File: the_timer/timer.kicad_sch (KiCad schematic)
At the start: 23 parts, among them J1 AVR-ISP-6, J2 Conn_01x04_Socket, J3 Conn_01x02_Socket, Q1 2N7002, Q2 2N7002, Q3 2N7002, U1 ATtiny48-A, U2 TPS61033, U3 MC3416, U4 W25Q128JVS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

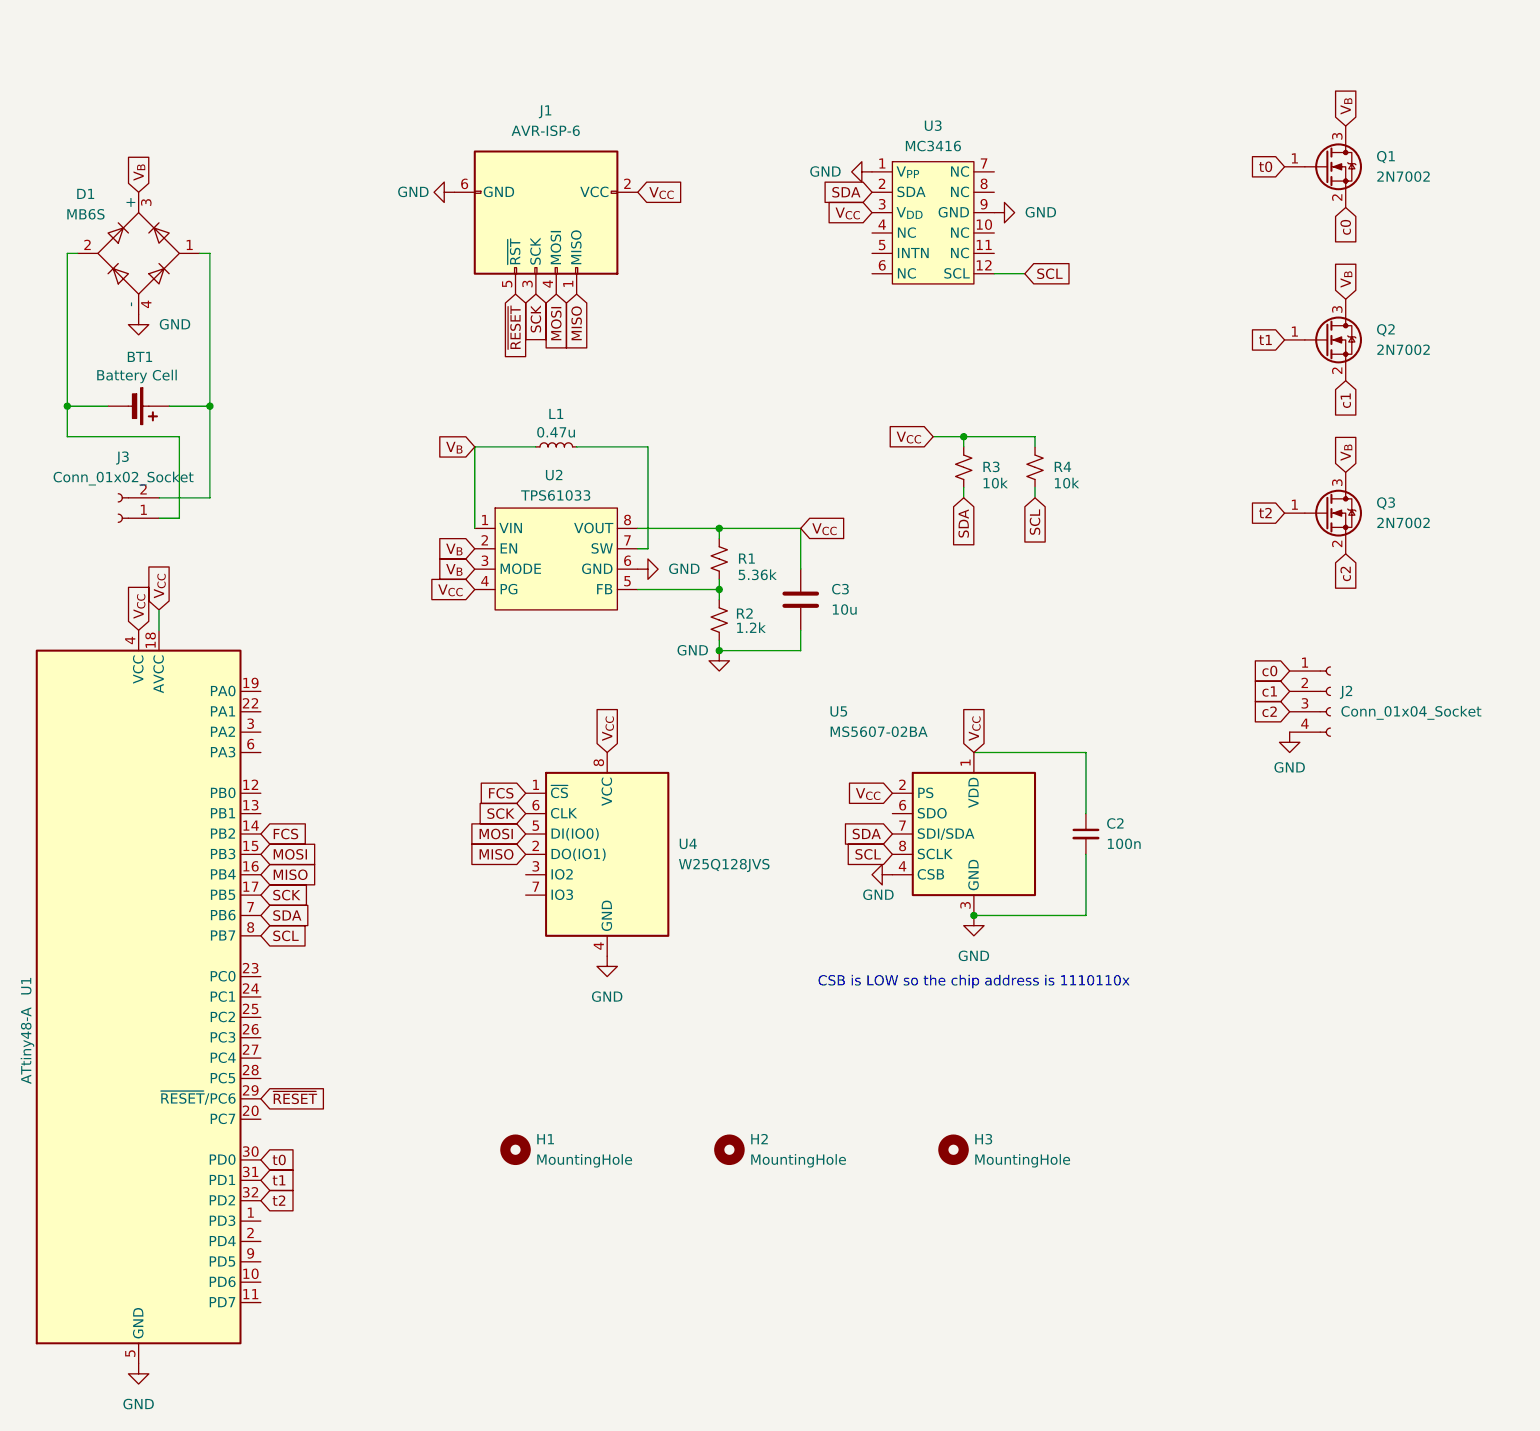
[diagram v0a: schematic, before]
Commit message: Replaced Timer mosfets
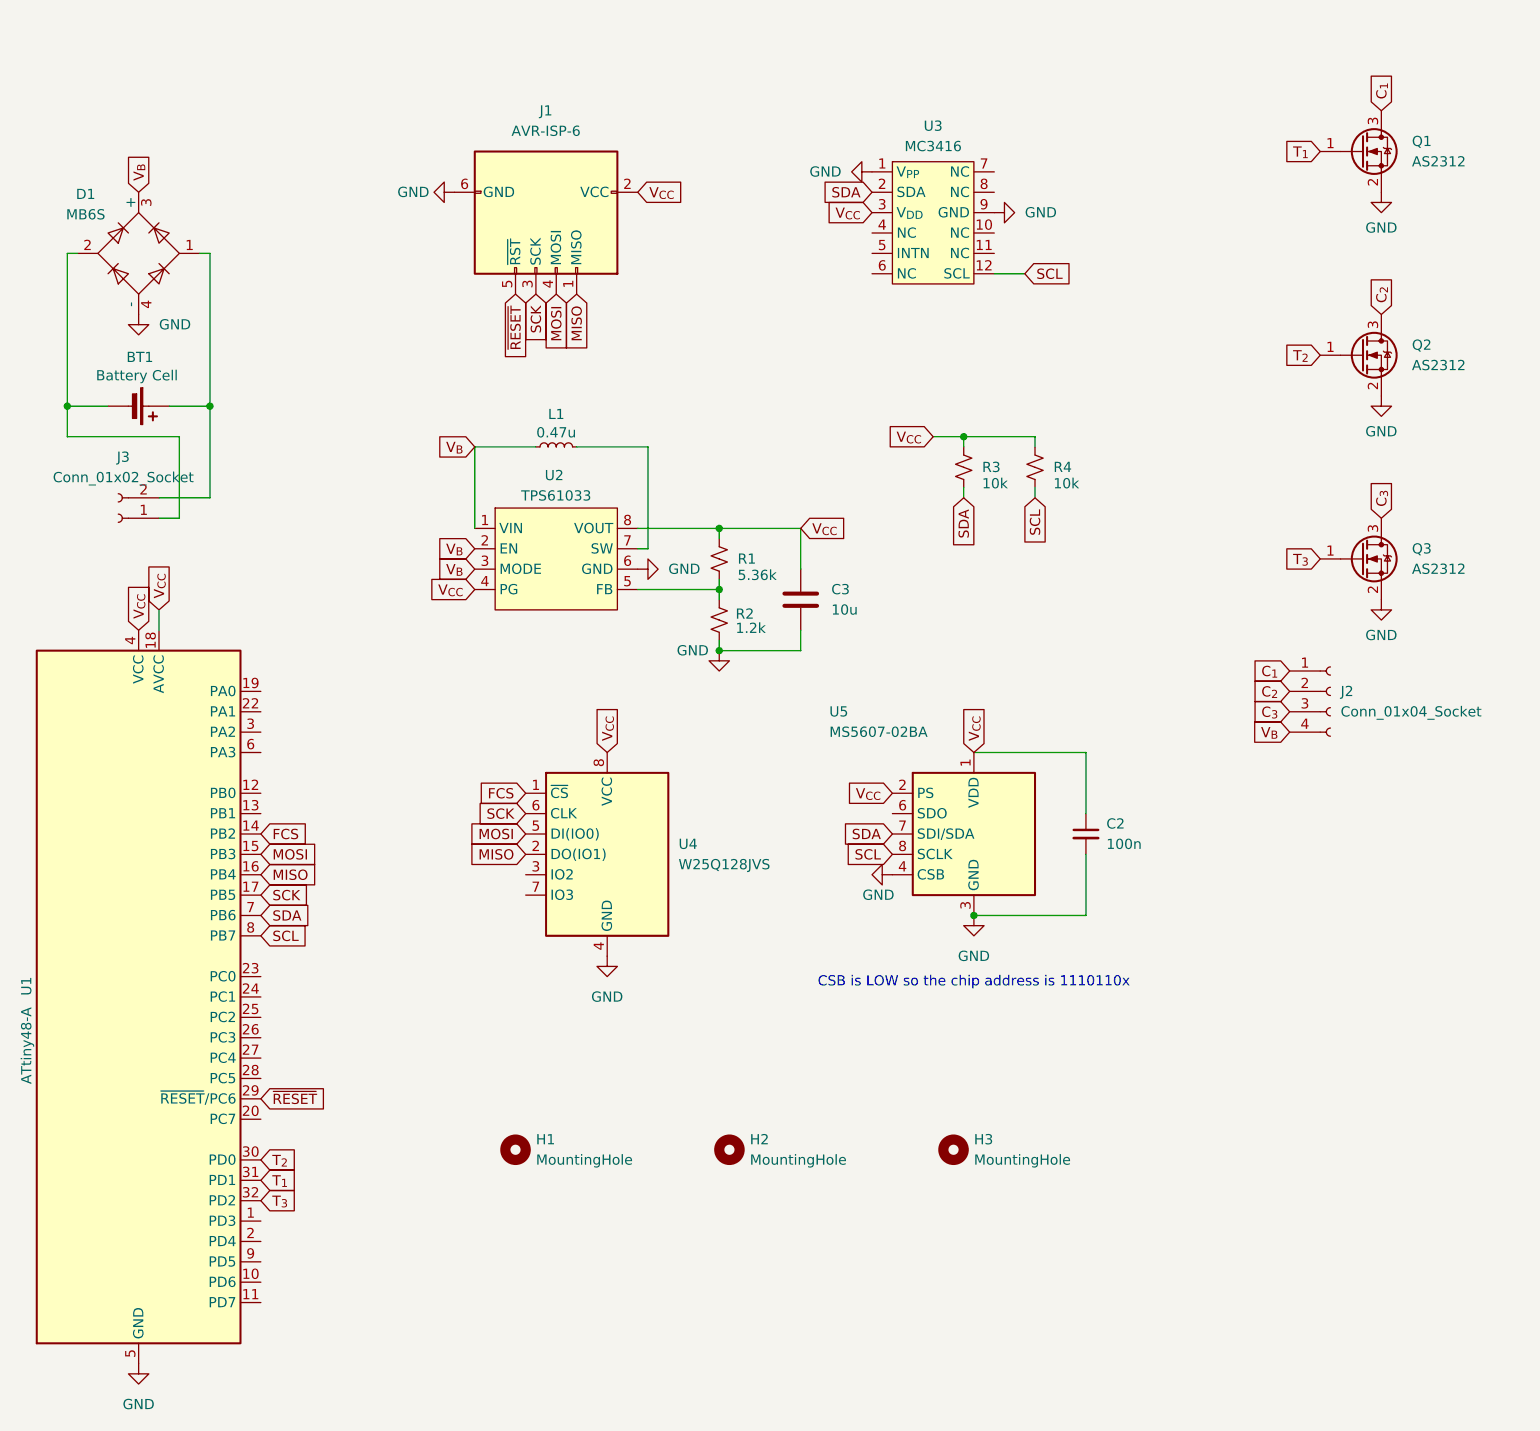
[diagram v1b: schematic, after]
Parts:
- Q1, Q2, Q3: value 2N7002 -> AS2312; DKPN 2N7002NCT-ND -> 4530-AS2312CT-ND
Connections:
- net GND: now also Q1.2 (S), Q2.2 (S), Q3.2 (S); no longer J2.4 (Pin_4)
- net V_{B}: now also J2.4 (Pin_4); no longer Q1.3 (D), Q2.3 (D), Q3.3 (D)
- net c0 renamed C_{1}
- net C_{1}: now also Q1.3 (D); no longer Q1.2 (S)
- net c1 renamed C_{2}
- net C_{2}: now also Q2.3 (D); no longer Q2.2 (S)
- net c2 renamed C_{3}
- net C_{3}: now also Q3.3 (D); no longer Q3.2 (S)
- net t0 renamed T_{1}
- net T_{1}: now also U1.31 (PD1); no longer U1.30 (PD0)
- net t1 renamed T_{2}
- net T_{2}: now also U1.30 (PD0); no longer U1.31 (PD1)
- net t2 renamed T_{3}
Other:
- moved on the sheet: Q1

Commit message: Generated Screamer and Timer BOMs
Both Screamer and Timer have been bumped to V0.1.
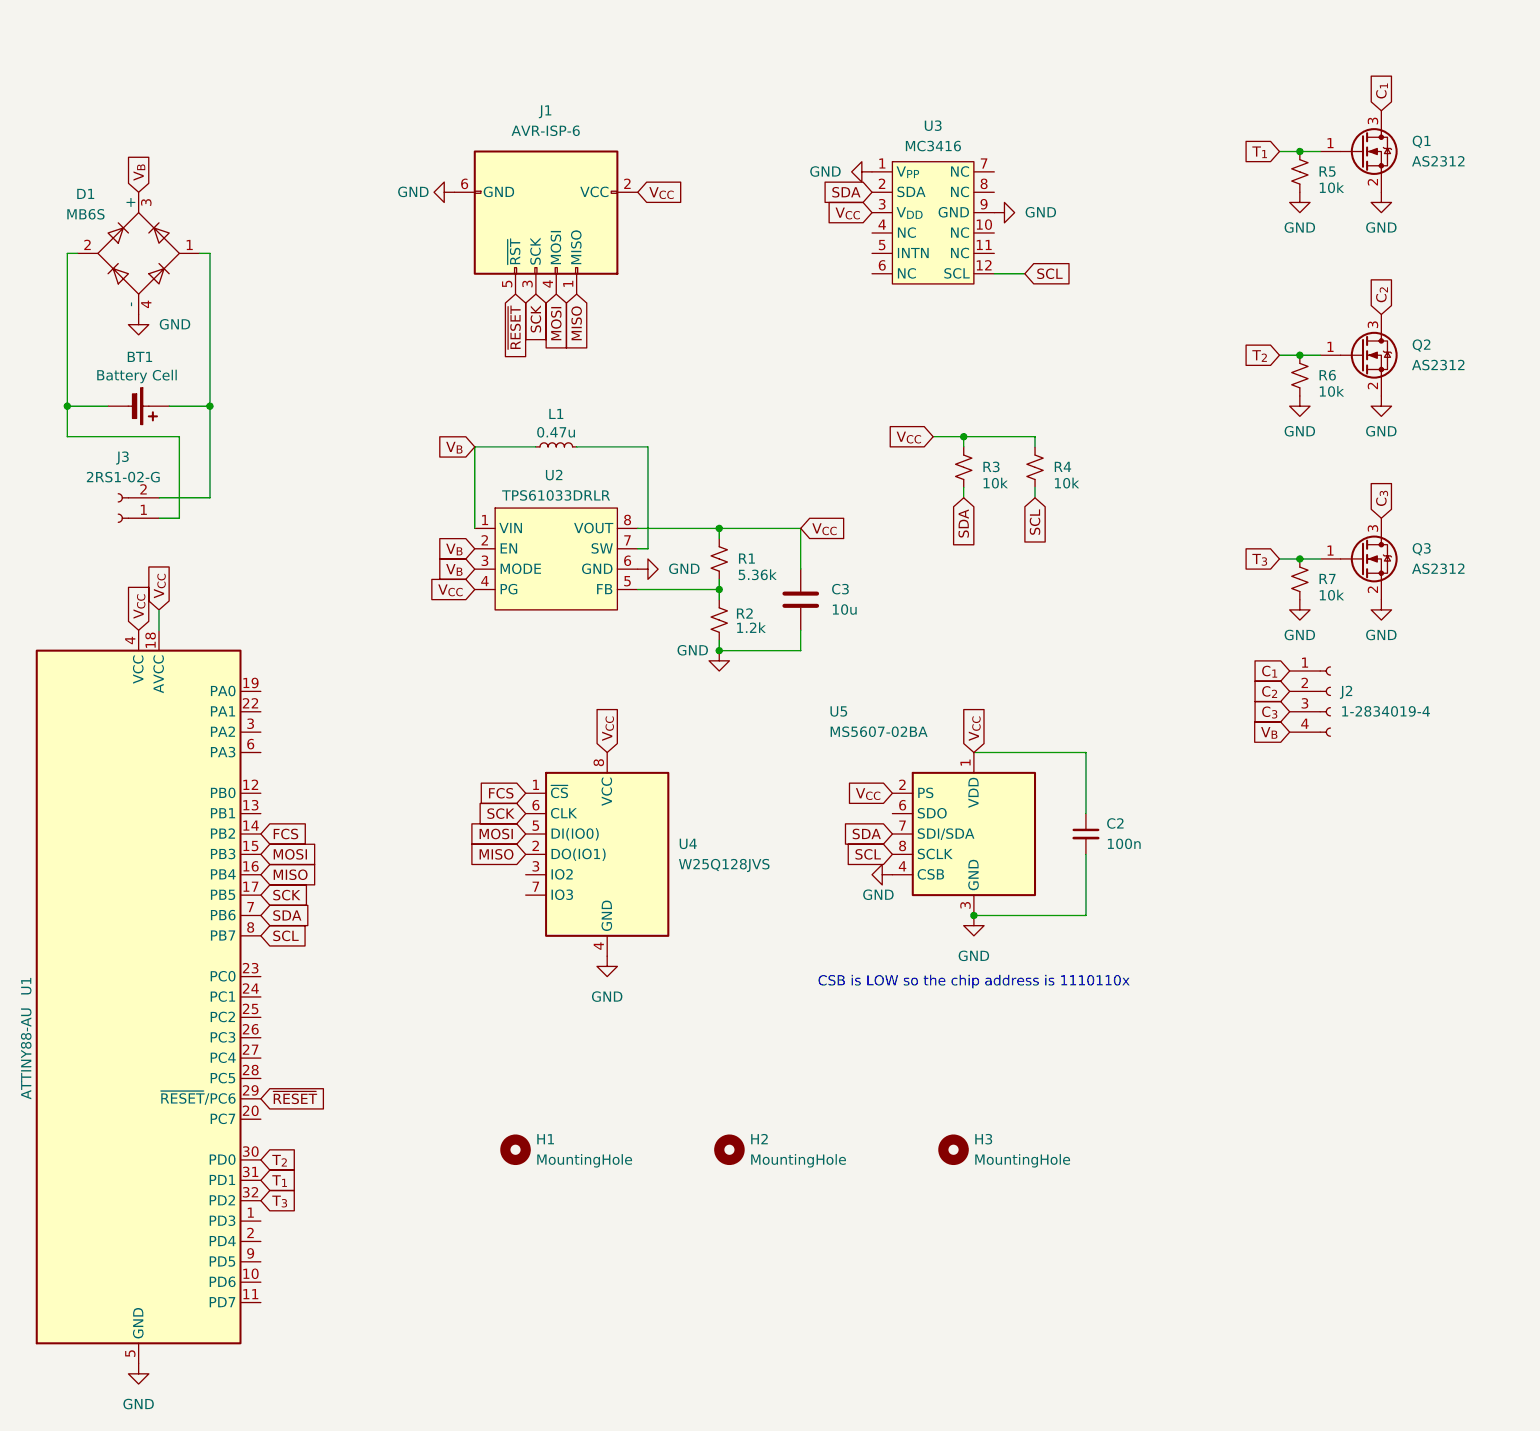
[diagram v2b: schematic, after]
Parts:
- added R5, R6, R7: 10k, Resistor_SMD:R_0603_1608Metric, symbol Device:R_Small_US
- C3: DKPN 490-12538-1-ND -> 732-7903-1-ND
- H1, H2, H3, J1: DKPN CONN -> (none)
- J2: value Conn_01x04_Socket -> 1-2834019-4; DKPN CONN -> A123842-ND
- J3: value Conn_01x02_Socket -> 2RS1-02-G; DKPN CONN -> 2057-2RS1-02-G-ND
- U1: value ATtiny48-A -> ATTINY88-AU; DKPN ATTINY48-AURCT-ND -> ATTINY88-AU-ND
- U2: value TPS61033 -> TPS61033DRLR; DKPN 296-TPS610333DRLRCT-ND -> 296-TPS61033DRLRCT-ND
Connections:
- net GND: now also R5.2, R6.2, R7.2
- net T_{1}: now also R5.1
- net T_{2}: now also R6.1
- net T_{3}: now also R7.1

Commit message: Fixed custom symbol file paths
In addition to fixing all the file paths I also updated some symbols on the Timer and Screamer, updated the board characteristic tables, added missing 3D models to some components, and did a bit of other file stuff.
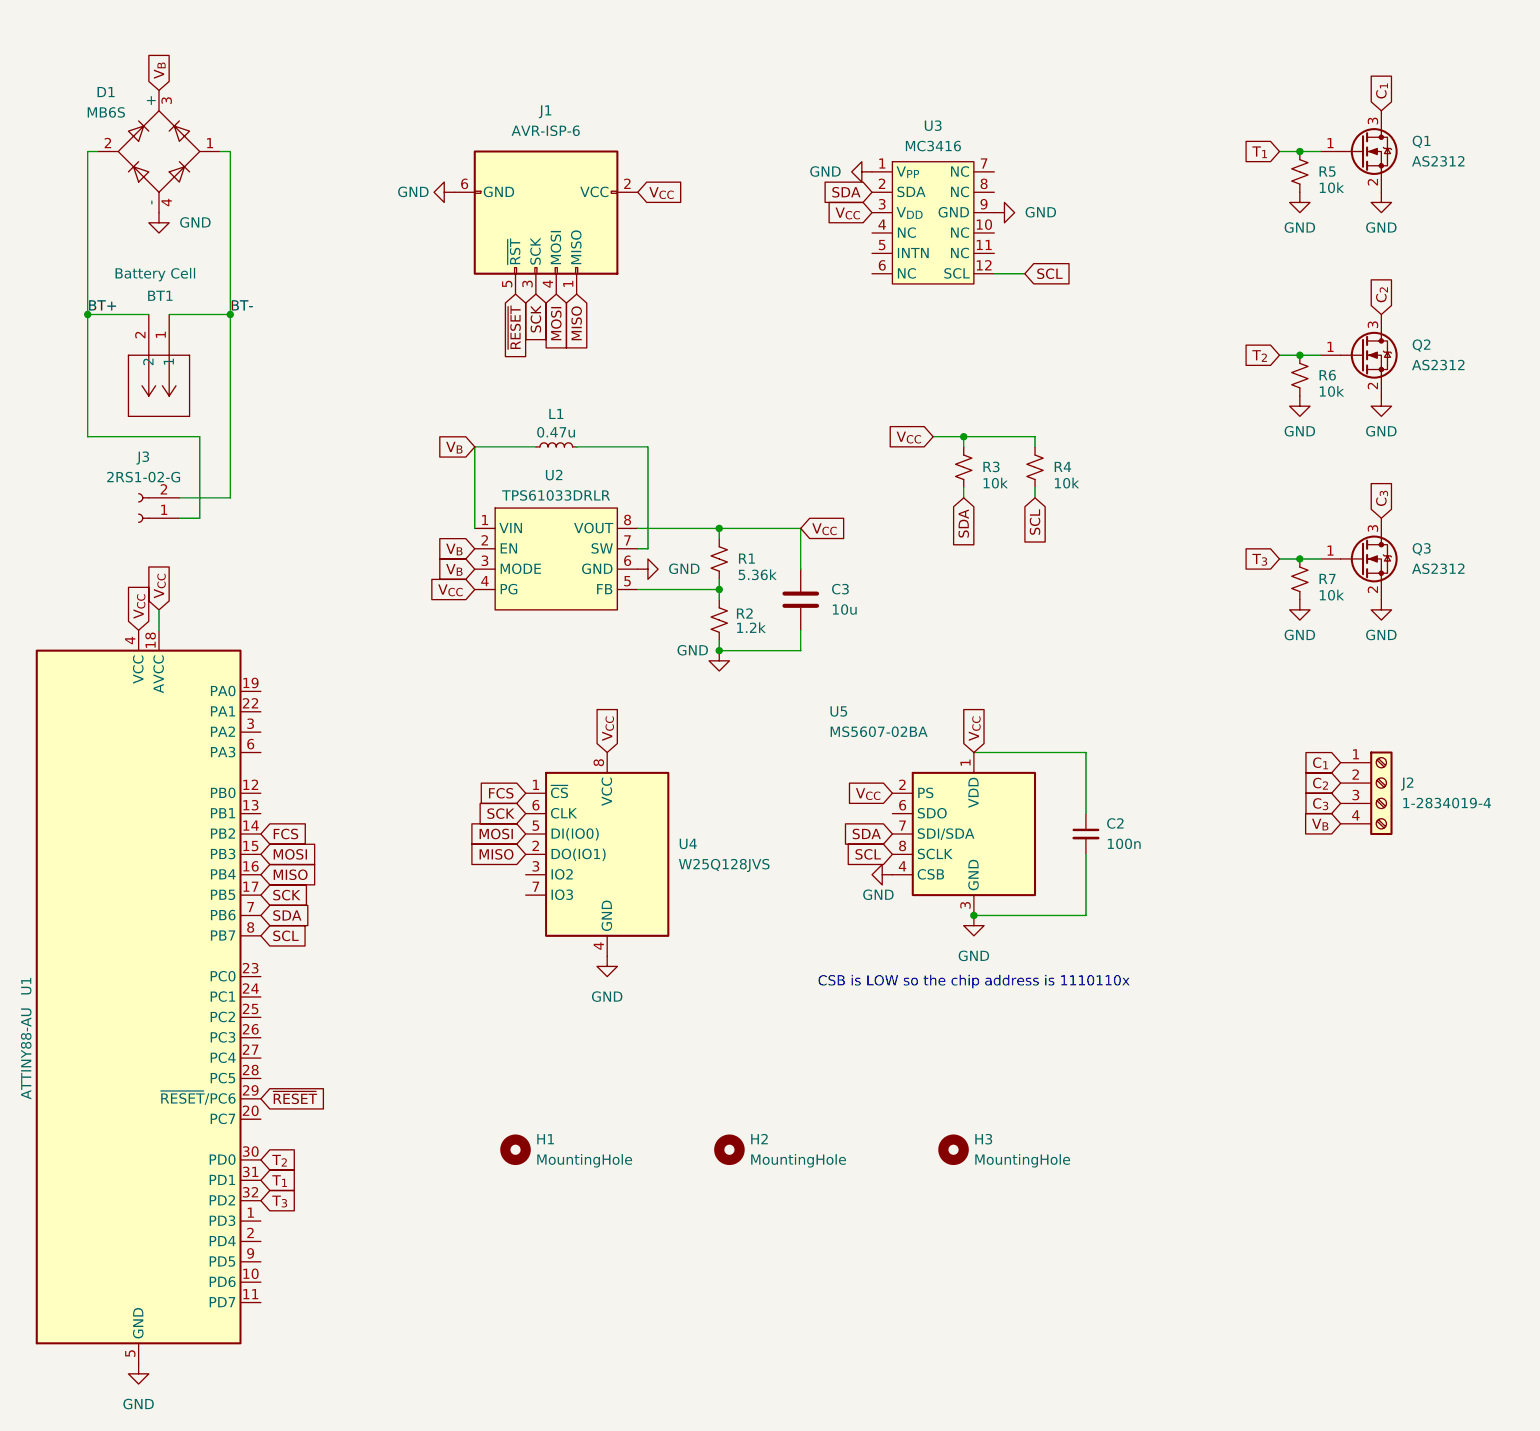
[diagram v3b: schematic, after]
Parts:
- BT1: symbol Device:Battery_Cell -> Custom_Flight_Computer_Symbols:1775469-2
- J2: footprint locals:TE_1-2834019-4 -> locals_but_working_PLEASE:TE_1-2834019-4; symbol Connector:Conn_01x04_Socket -> Custom_Flight_Computer_Symbols:1-2834019-4
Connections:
- net BT+: now reaches BT1.2, D1.2, J3.1 (Pin_1)
- net BT-: now reaches BT1.1, D1.1, J3.2 (Pin_2)
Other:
- moved on the sheet: D1, J3

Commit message: Redesigned Timer Programmer
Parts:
- J1: DKPN (none) -> 2057-HPH2-A-06-UA-ND
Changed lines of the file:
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@@
 	(title_block
 		(title "Timer")
-		(date "2024-05-16")
-		(rev "V0.1.4")
+		(date "2024-05-26")
+		(rev "V0.1.5")
 		(company "Mines Rocket Club")
 		(comment 1 "William Layne")
@@
 			)
 		)
-		(property "DKPN" ""
+		(property "DKPN" "2057-HPH2-A-06-UA-ND"
 			(at 85.09 33.02 0)
 			(effects
